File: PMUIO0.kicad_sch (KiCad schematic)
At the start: 3 parts

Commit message: added README and license
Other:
- company: (none) -> Yang Hongbo
- title: (none) -> Leaf RV1126
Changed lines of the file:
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@@
 (kicad_sch (version 20230121) (generator eeschema)
   (paper "A4")
+  (title_block
+    (title "Leaf RV1126")
+    (date "2023-06-07")
+    (company "Yang Hongbo")
+    (comment 1 "License: CC BY-SA")
+  )
   (junction (at 195.58 99.06) (diameter 0) (color 0 0 0 0)
   )

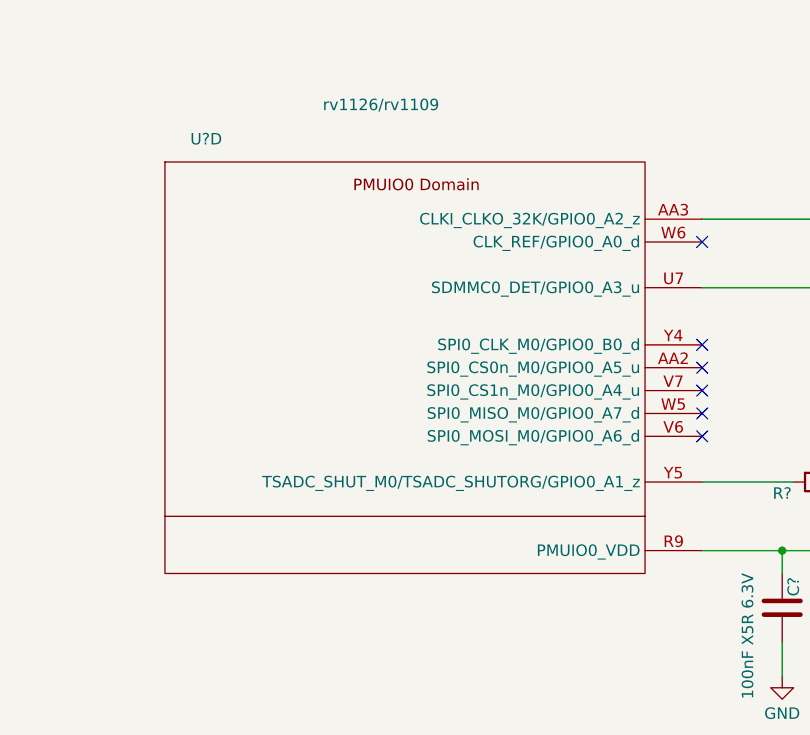
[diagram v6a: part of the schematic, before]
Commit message: replaced Leaf specified symbols with unified iotpi symbols
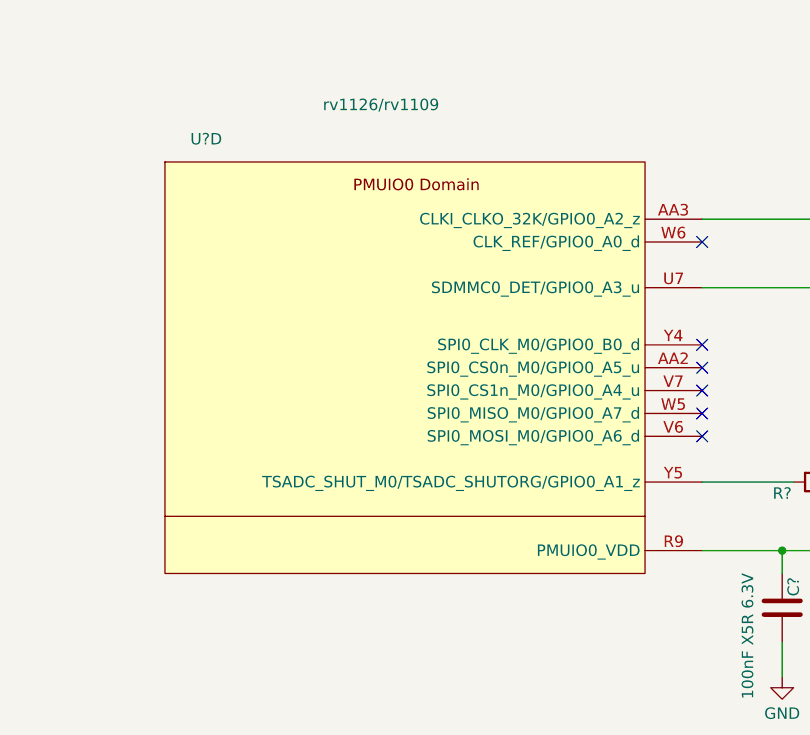
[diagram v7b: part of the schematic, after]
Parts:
- U?: symbol CPU_Rockchip:rv1126_rv1109 -> IotPi_CPU_Rockchip:rv1126_rv1109
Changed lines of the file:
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@@
     )
   )
-  (symbol (lib_id "CPU_Rockchip:rv1126_rv1109") (at 153.67 77.47 0) (unit 4)
+  (symbol (lib_id "IotPi_CPU_Rockchip:rv1126_rv1109") (at 153.67 77.47 0) (unit 4)
     (in_bom yes) (on_board yes) (dnp no)
     (property "Reference" "U?" (at 133.35 53.34 0)
@@
       (effects (font (size 1.27 1.27)) (justify right))
     )
-    (property "Footprint" "Rockchip_SoC:Rockchip_RV1126_FCCSP409LD_14.0x14.0mm" (at 180.34 104.14 0)
+    (property "Footprint" "Rockchip_SoC:Rockchip_RV1126_FCCSP409LD_14.0x14.0mm" (at 185.42 124.46 0)
       (effects (font (size 1.27 1.27)) hide)
     )
-    (property "Datasheet" "" (at 180.34 104.14 0)
+    (property "Datasheet" "" (at 185.42 124.46 0)
       (effects (font (size 1.27 1.27)) hide)
     )

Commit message: replaced Leaf libraries with combined libraries
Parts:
- U?: footprint Rockchip_SoC:Rockchip_RV1126_FCCSP409LD_14.0x14.0mm -> IotPi_Rockchip_SoC:Rockchip_RV1126_FCCSP409LD_14.0x14.0mm
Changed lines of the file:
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@@
       (effects (font (size 1.27 1.27)) (justify right))
     )
-    (property "Footprint" "Rockchip_SoC:Rockchip_RV1126_FCCSP409LD_14.0x14.0mm" (at 185.42 124.46 0)
+    (property "Footprint" "IotPi_Rockchip_SoC:Rockchip_RV1126_FCCSP409LD_14.0x14.0mm" (at 185.42 124.46 0)
       (effects (font (size 1.27 1.27)) hide)
     )
